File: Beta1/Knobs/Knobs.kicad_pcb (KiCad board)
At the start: 2 copper layers, 194 x 30.9 mm, 38 parts, among them U1000 MCP3008T-I/SL, U2 MCP3008T-I/SL

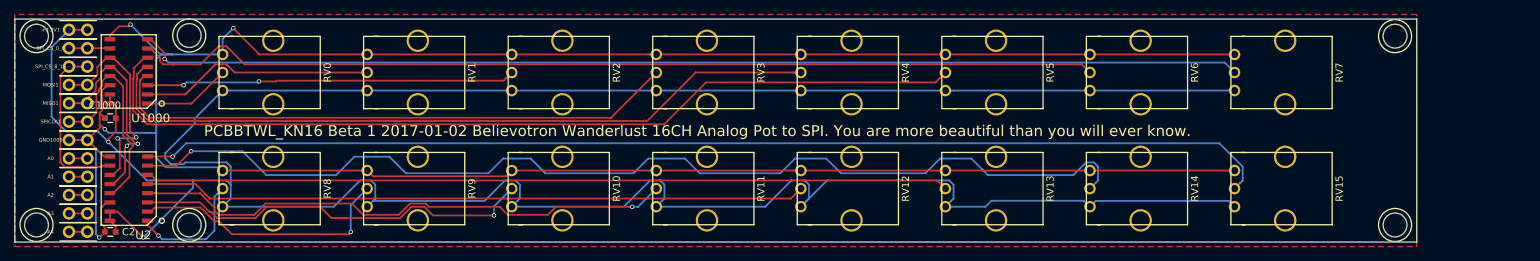
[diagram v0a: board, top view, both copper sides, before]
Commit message: Added volume knob + XY Joy to Knobs 16 CH Board.
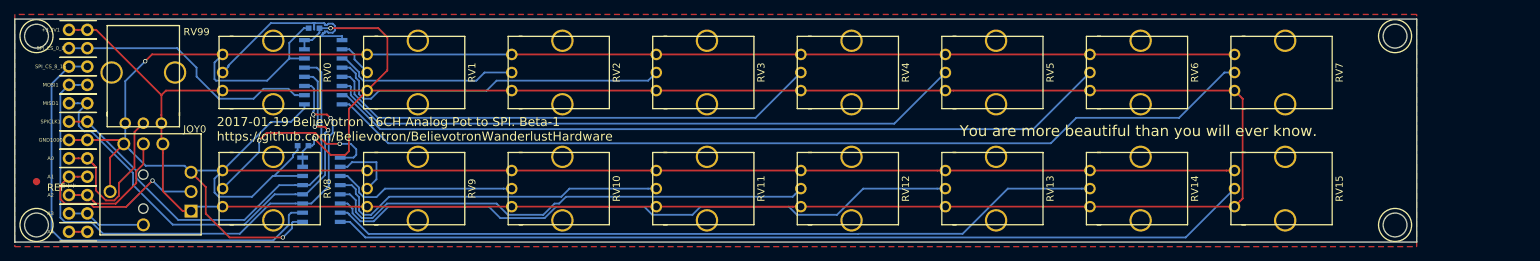
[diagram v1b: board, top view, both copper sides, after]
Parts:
- removed the REF** at (24.1, -29.2)
- removed the REF** at (24.1, -3.00)
- added JOY0: XYJOY, Liberry:XY_JOY_254TA103B50B, F.Cu at (17.8, -7.62)
- added REF**: Fiducial_1mm_Dia_2.54mm_Outer_CopperTop, Fiducials:Fiducial_1mm_Dia_2.54mm_Outer_CopperTop, F.Cu at (3.05, -8.89)
- added RV99: POT, Liberry:RV09AF-40-20K-B10K, F.Cu at (17.8, -24.1)
- C1000, C2, U1000, U2: moved to B.Cu
- moved C1000 30.8 mm to (41.4, -30.2)
- moved C2 29.2 mm to (39.9, -14.0)
- moved U1000 26.9 mm to (42.7, -24.1), turned to 270 degrees
- moved U2 26.7 mm to (42.4, -7.87), turned to 270 degrees
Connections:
- A0 pad 1: Net-(A0-Pad1) -> /VOLUME
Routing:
- net (no net): track 235.6 -> 0.00 mm
- net /MOSI: track 29.3 -> 79.6 mm
- net GND: track 374.9 -> 419.0 mm, vias 4 -> 2
- net /CS_LED_8_15: track 23.5 -> 63.9 mm
- net /P14: track 147.0 -> 107.6 mm, vias 1 -> 0
- net /MISO: track 29.9 -> 66.7 mm
- net /P5: track 124.5 -> 89.2 mm
- net /P4: track 102.1 -> 69.5 mm
- net /P3: track 79.7 -> 48.2 mm
- net /CS_R0_7: track 5.69 -> 37.1 mm
- net /SPICLK: track 29.7 -> 60.4 mm
- net /P10: track 56.0 -> 25.8 mm, vias 1 -> 0
- net /P15: track 157.1 -> 127.4 mm, vias 1 -> 0
- net /P1: track 32.9 -> 5.24 mm
- net /P11: track 76.0 -> 48.4 mm, vias 1 -> 0
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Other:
- board text added: "2017-01-19 Believotron 16CH Analog Pot to SPI. Beta-1 https://github.com/Believotron/BelievotronWanderlustHardware"
- board text added: "You are more beautiful than you will ever know."
- board text removed: "PCBBTWL_KN16 Beta 1 2017-01-02 Believotron Wanderlust 16CH Analog Pot to SPI. You are more beautiful than you will ever know."

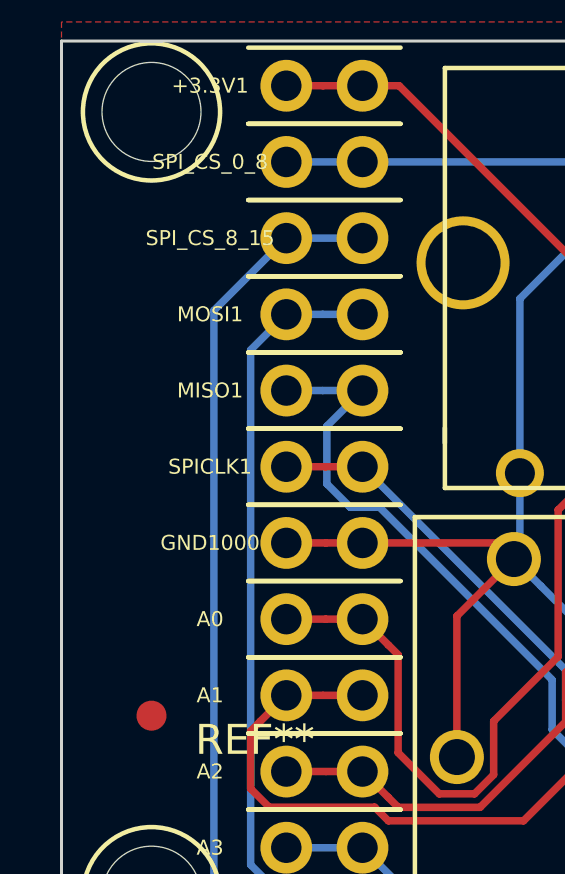
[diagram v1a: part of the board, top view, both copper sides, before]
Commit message: Added Website URL top Knobs PCB
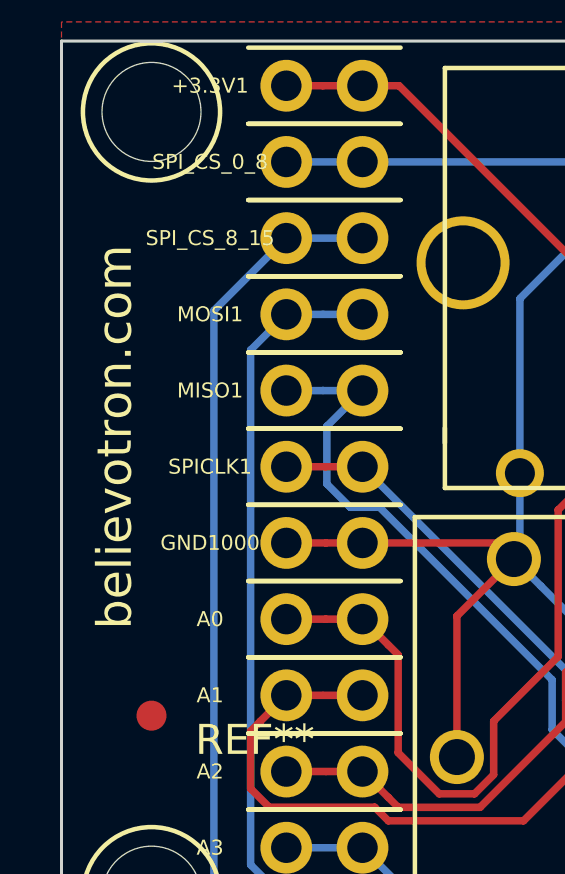
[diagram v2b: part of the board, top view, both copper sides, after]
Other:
- board text added: "believotron.com"
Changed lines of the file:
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@@
     (area -0.050001 -31.537501 194.010001 -0.587499)
     (thickness 1.6)
-    (drawings 16)
+    (drawings 17)
     (tracks 423)
     (zones 0)
@@
       (solder_mask_margin 0.77) (clearance 0.77))
   )
+  (gr_text believotron.com (at 1.778 -18.288 90) (layer F.SilkS)
+    (effects (font (size 1.15 1.15) (thickness 0.2875)))
+  )
   (gr_text "You are more beautiful than you will ever know." (at 155.448 -16.002) (layer F.SilkS)

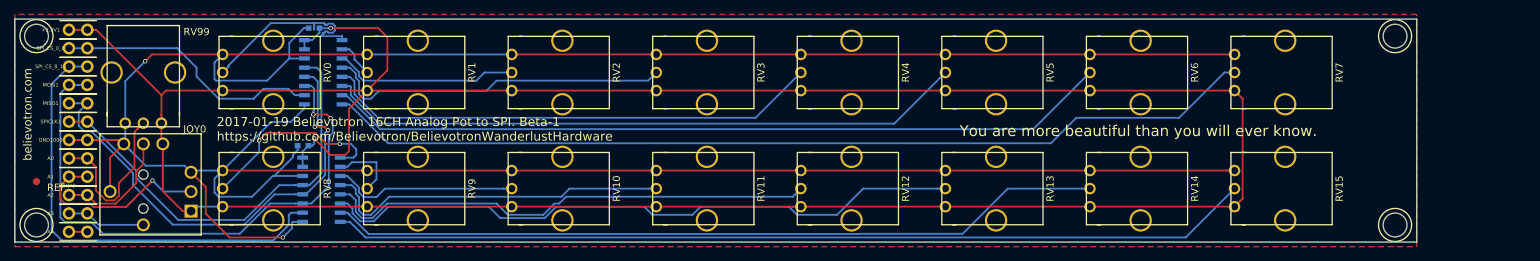
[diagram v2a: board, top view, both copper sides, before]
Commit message: Reduced width by 5.08. Changed pinout location and organization
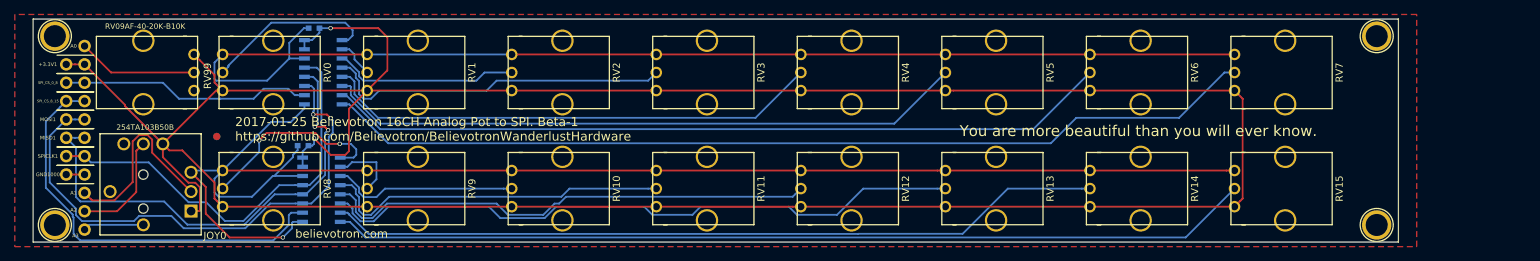
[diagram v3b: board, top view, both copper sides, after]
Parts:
- removed A4: CONN_01X01, Liberry:TH_0.1_1x2_Jumper
- added REF**: Fiducial_1mm_Dia_2.54mm_Outer_CopperBottom, Fiducials:Fiducial_1mm_Dia_2.54mm_Outer_CopperBottom, F.Cu at (27.9, -15.2)
- A0, A1, A2, A3: footprint Liberry:TH_0.1_1x2_Jumper -> Liberry:single_0.1
- moved REF** 25.7 mm to (27.9, -15.2)
- moved A0 15.7 mm to (9.65, -27.8)
- moved MOSI1 4.79 mm to (7.11, -17.6)
- moved GND1000 4.79 mm to (7.11, -9.98)
- moved +3.3V1 4.79 mm to (7.11, -25.2)
- moved MISO1 4.79 mm to (7.11, -15.1)
- moved SPICLK1 4.79 mm to (7.11, -12.5)
- moved SPI_CS_0_8 4.79 mm to (7.11, -22.7)
- moved SPI_CS_8_15 4.79 mm to (7.11, -20.1)
- moved A1 3.11 mm to (9.65, -7.44)
- moved A2 3.11 mm to (9.65, -4.90)
- moved A3 3.11 mm to (9.65, -2.36)
- moved REF** 2.54 mm to (188.4, -29.1)
- moved REF** 2.54 mm to (188.4, -3.00)
- moved REF** 2.54 mm to (5.54, -3.00)
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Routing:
- net GND: track 419.0 -> 372.7 mm, vias 2 -> 1
- net +3V3: track 388.4 -> 403.6 mm
- net /VOLUME: track 22.9 -> 16.7 mm
- net /CS_LED_8_15: track 63.9 -> 58.1 mm
- net /MOSI: track 79.6 -> 74.4 mm
- net /P0: track 27.3 -> 23.8 mm
- net Net-(A4-Pad1): track 2.54 -> 0.00 mm
- net Net-(A3-Pad1): track 10.9 -> 8.40 mm
- net /SPICLK: track 60.4 -> 58.3 mm
- net /CS_R0_7: track 37.1 -> 35.1 mm
- net Net-(A2-Pad1): track 16.8 -> 15.3 mm
- net Net-(A1-Pad1): track 26.8 -> 26.5 mm, vias 1 -> 0
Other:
- board size 194 x 30.9 mm -> 188.9 x 30.9 mm
- board text added: "2017-01-25 Believotron 16CH Analog Pot to SPI. Beta-1 https://github.com/Believotron/BelievotronWanderlustHardware"
- board text added: "254TA103B50B"
- board text added: "MCP3008T-I/SL"
- board text added: "RV09AF-40-20K-B10K"
- board text removed: "2017-01-19 Believotron 16CH Analog Pot to SPI. Beta-1 https://github.com/Believotron/BelievotronWanderlustHardware"

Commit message: Fixed trace
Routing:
- net GND: track 372.7 -> 377.8 mm
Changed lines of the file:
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@@
   (general
     (links 86)
-    (no_connects 13)
-    (area 2.489999 -31.537501 191.470001 -0.587499)
+    (no_connects 1)
+    (area 0 -33.148 193.960001 1.255473)
     (thickness 1.6)
     (drawings 20)
-    (tracks 388)
+    (tracks 391)
     (zones 0)
     (modules 39)
@@
     (effects (font (size 1.5 1.5) (thickness 0.3)) (justify mirror))
   )
-  (gr_text believotron.com (at 45.212 -1.778 360) (layer F.SilkS)
+  (gr_text believotron.com (at 45.212 -1.778) (layer F.SilkS)
     (effects (font (size 1.15 1.15) (thickness 0.2875)))
   )
@@
   (gr_line (start 2.54 -0.6375) (end 2.54 -31.4875) (layer Edge.Cuts) (width 0.1))
   (gr_line (start 2.54 -0.6375) (end 191.42 -0.6375) (layer Edge.Cuts) (width 0.1))
+  (segment (start 28.7496 -26.594) (end 27.624599 -25.468999) (width 0.25) (layer B.Cu) (net 1))
+  (segment (start 27.624599 -25.468999) (end 27.624599 -24.428199) (width 0.25) (layer B.Cu) (net 1))
+  (segment (start 27.624599 -24.428199) (end 25.590399 -22.393999) (width 0.25) (layer B.Cu) (net 1))
+  (segment (start 25.590399 -22.393999) (end 24.7904 -21.594) (width 0.25) (layer B.Cu) (net 1))
   (segment (start 14.5426 -14.7574) (end 15.08 -14.22) (width 0.25) (layer F.Cu) (net 1))
   (segment (start 48.7496 -26.594) (end 68.7496 -26.594) (width 0.25) (layer B.Cu) (net 1))
@@
   (segment (start 27.624599 -23.175401) (end 27.831001 -22.968999) (width 0.25) (layer B.Cu) (net 1))
   (segment (start 27.831001 -22.968999) (end 34.906999 -22.968999) (width 0.25) (layer B.Cu) (net 1))
-  (segment (start 28.7496 -26.594) (end 27.624599 -25.468999) (width 0.25) (layer B.Cu) (net 1))
   (segment (start 27.624599 -25.468999) (end 27.624599 -23.175401) (width 0.25) (layer B.Cu) (net 1))
   (segment (start 9.649605 -9.979527) (end 8.428291 -9.979527) (width 0.25) (layer F.Cu) (net 1))
